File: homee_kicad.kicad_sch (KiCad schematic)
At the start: 22 parts, among them J1 Screw_Terminal_01x02, J2 476421001, J3 Screw_Terminal_01x02, K1 ORWH-SH-105D1F,000, Q1 2N7002, U1 ESP-01v090, U2 LD1117S33TR_SOT223, U4 PC817

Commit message: schema final rework
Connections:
- net 5V is gone; now on net +5V: BC1.3 (VCC_OUT), C1.2, D7.1 (K), K1.2 (COIL_1), R9.2, U2.3 (VI)
- net GND: now also Q1.2 (S); no longer Q1.3 (D)
- net at D7.2 (A), D8.1 (K), K1.4 (COIL_2): now also Q1.3 (D); no longer Q1.2 (S)
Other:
- moved on the sheet: D7, D8, J3, K1, Q1, R7, R8, R9, U4

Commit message: oupsi
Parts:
- BC1: footprint Connect:Buck Connect -> Homme:Buck Connect
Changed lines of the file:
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@@
 			)
 		)
-		(property "Footprint" "Connect:Buck Connect"
+		(property "Footprint" "Homme:Buck Connect"
 			(at 140.97 130.81 0)
 			(effects

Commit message: Change IO disposition
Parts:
- removed J1, J3: Screw_Terminal_01x02, TerminalBlock_Phoenix:TerminalBlock_Phoenix_MKDS-1,5-2-5.08_1x02_P5.08mm_Horizontal, symbol Connector:Screw_Terminal_01x02
- removed K1: ORWH-SH-105D1F,000, Homme:ORWH-1T, symbol ORWH-SH-105D1F_000:ORWH-SH-105D1F,000
- added J1: Screw_Terminal_01x04, symbol Connector:Screw_Terminal_01x04
- added K2: SANYOU_SRD_Form_C, Relay_THT:Relay_SPDT_SANYOU_SRD_Series_Form_C, symbol Relay:SANYOU_SRD_Form_C
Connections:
- net +5V: now also K2.2
- net L IN: now also J1.3 (Pin_3), K2.1
- net N IN: now also J1.1 (Pin_1)
- net at D7.2 (A), D8.1 (K), Q1.3 (D): now also K2.5
- new net NC: J1.2 (Pin_2), K2.4
- new net NO: J1.4 (Pin_4), K2.3

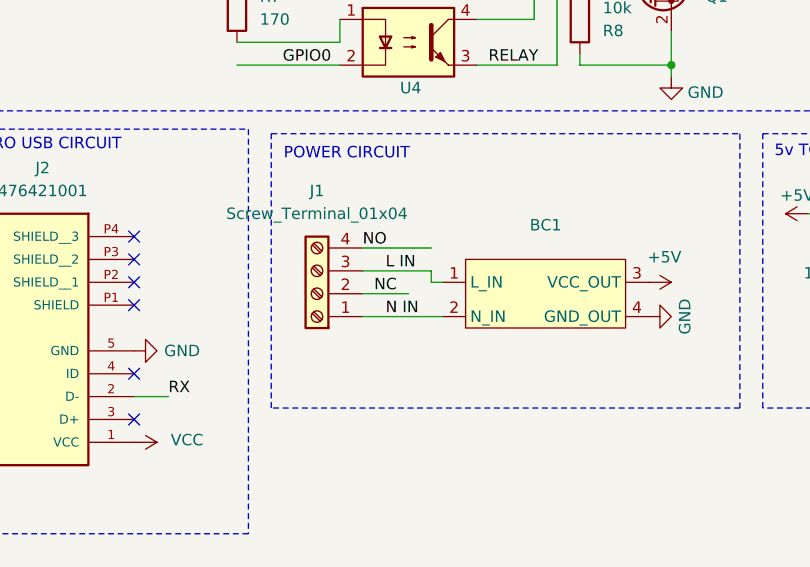
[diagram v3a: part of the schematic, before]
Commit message: UPDATED TEST W/O ROUTES
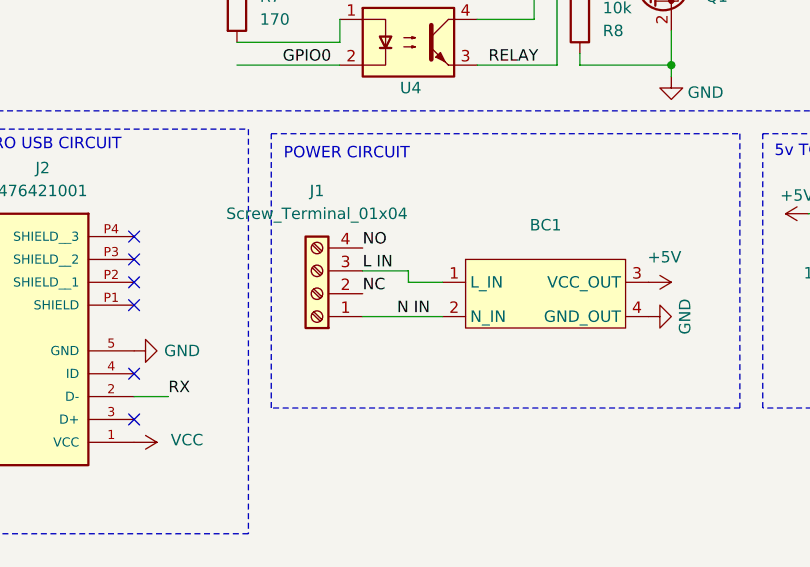
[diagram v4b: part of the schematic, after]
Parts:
- J1: footprint (none) -> TerminalBlock_Phoenix:TerminalBlock_Phoenix_PT-1,5-4-3.5-H_1x04_P3.50mm_Horizontal
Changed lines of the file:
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@@
+	(wire
+		(pts
+			(xy 124.46 139.7) (xy 133.35 139.7)
+		)
+		(stroke
+			(width 0)
+			(type default)
+		)
+	)
 	(wire
 		(pts
@@
 	(wire
 		(pts
-			(xy 132.08 132.08) (xy 124.46 132.08)
-		)
-		(stroke
-			(width 0)
-			(type default)
-		)
-	)
-	(wire
-		(pts
 			(xy 179.07 60.96) (xy 179.07 66.04)
 		)
@@
 	(wire
 		(pts
-			(xy 132.08 135.89) (xy 133.35 135.89)
-		)
-		(stroke
-			(width 0)
-			(type default)
-		)
-	)
-	(wire
-		(pts
-			(xy 132.08 134.62) (xy 132.08 135.89)
-		)
-		(stroke
-			(width 0)
-			(type default)
-		)
-	)
-	(wire
-		(pts
 			(xy 158.75 111.76) (xy 158.75 107.95)
 		)
@@
 	(wire
 		(pts
-			(xy 124.46 139.7) (xy 133.35 139.7)
-		)
-		(stroke
-			(width 0)
-			(type default)
-		)
-	)
-	(wire
-		(pts
 			(xy 148.59 102.87) (xy 151.13 102.87)
 		)
@@
 	(wire
 		(pts
+			(xy 129.54 135.89) (xy 133.35 135.89)
+		)
+		(stroke
+			(width 0)
+			(type default)
+		)
+	)
+	(wire
+		(pts
 			(xy 148.59 102.87) (xy 146.05 102.87)
 		)
@@
 	(wire
 		(pts
-			(xy 124.46 134.62) (xy 132.08 134.62)
-		)
-		(stroke
-			(width 0)
-			(type default)
-		)
-	)
-	(wire
-		(pts
 			(xy 110.49 109.22) (xy 121.92 109.22)
 		)
@@
 	(wire
 		(pts
-			(xy 129.54 137.16) (xy 124.46 137.16)
-		)
-		(stroke
-			(width 0)
-			(type default)
-		)
-	)
-	(wire
-		(pts
 			(xy 191.77 110.49) (xy 191.77 107.95)
 		)
@@
 		(pts
 			(xy 158.75 86.36) (xy 158.75 82.55)
+		)
+		(stroke
+			(width 0)
+			(type default)
+		)
+	)
+	(wire
+		(pts
+			(xy 129.54 134.62) (xy 129.54 135.89)
+		)
+		(stroke
+			(width 0)
+			(type default)
+		)
+	)
+	(wire
+		(pts
+			(xy 124.46 134.62) (xy 129.54 134.62)
 		)
 		(stroke
@@
 	)
 	(label "NC"
-		(at 125.73 137.16 0)
-		(fields_autoplaced yes)
-		(effects
-			(font
-				(size 1.27 1.27)
-			)
-			(justify left bottom)
-		)
-	)
-	(label "N IN"
-		(at 127 139.7 0)
+		(at 124.46 137.16 0)
 		(fields_autoplaced yes)
 		(effects
@@
 	)
 	(label "L IN"
-		(at 127 134.62 0)
+		(at 124.46 134.62 0)
+		(fields_autoplaced yes)
+		(effects
+			(font
+				(size 1.27 1.27)
+			)
+			(justify left bottom)
+		)
+	)
+	(label "N IN"
+		(at 128.27 139.7 0)
 		(fields_autoplaced yes)
 		(effects
@@
 			)
 		)
-		(property "Footprint" ""
+		(property "Footprint" "TerminalBlock_Phoenix:TerminalBlock_Phoenix_PT-1,5-4-3.5-H_1x04_P3.50mm_Horizontal"
 			(at 119.38 137.16 0)
 			(effects

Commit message: JOB'S FINISHED ? JOB'S NOT FINISHED
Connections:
- net L IN: now also J1.2 (Pin_2); no longer J1.3 (Pin_3)
- net N IN: now also J1.4 (Pin_4); no longer J1.1 (Pin_1)
- net NC: now also J1.3 (Pin_3); no longer J1.2 (Pin_2)
- net NO: now also J1.1 (Pin_1); no longer J1.4 (Pin_4)
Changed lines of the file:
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@@
-	(wire
-		(pts
-			(xy 124.46 139.7) (xy 133.35 139.7)
-		)
-		(stroke
-			(width 0)
-			(type default)
-		)
-	)
 	(wire
 		(pts
@@
 	(wire
 		(pts
-			(xy 129.54 135.89) (xy 133.35 135.89)
-		)
-		(stroke
-			(width 0)
-			(type default)
-		)
-	)
-	(wire
-		(pts
 			(xy 148.59 102.87) (xy 146.05 102.87)
 		)
@@
 	(wire
 		(pts
+			(xy 133.35 137.16) (xy 133.35 135.89)
+		)
+		(stroke
+			(width 0)
+			(type default)
+		)
+	)
+	(wire
+		(pts
 			(xy 179.07 55.88) (xy 184.15 55.88)
 		)
@@
 	(wire
 		(pts
+			(xy 124.46 137.16) (xy 133.35 137.16)
+		)
+		(stroke
+			(width 0)
+			(type default)
+		)
+	)
+	(wire
+		(pts
 			(xy 146.05 102.87) (xy 146.05 111.76)
 		)
@@
 	(wire
 		(pts
+			(xy 124.46 132.08) (xy 130.81 132.08)
+		)
+		(stroke
+			(width 0)
+			(type default)
+		)
+	)
+	(wire
+		(pts
 			(xy 143.51 101.6) (xy 143.51 106.68)
 		)
@@
 	(wire
 		(pts
+			(xy 130.81 139.7) (xy 133.35 139.7)
+		)
+		(stroke
+			(width 0)
+			(type default)
+		)
+	)
+	(wire
+		(pts
 			(xy 110.49 109.22) (xy 121.92 109.22)
 		)
@@
 	(wire
 		(pts
+			(xy 130.81 132.08) (xy 130.81 139.7)
+		)
+		(stroke
+			(width 0)
+			(type default)
+		)
+	)
+	(wire
+		(pts
 			(xy 176.53 128.27) (xy 176.53 133.35)
 		)
@@
 		(pts
 			(xy 158.75 86.36) (xy 158.75 82.55)
-		)
-		(stroke
-			(width 0)
-			(type default)
-		)
-	)
-	(wire
-		(pts
-			(xy 129.54 134.62) (xy 129.54 135.89)
-		)
-		(stroke
-			(width 0)
-			(type default)
-		)
-	)
-	(wire
-		(pts
-			(xy 124.46 134.62) (xy 129.54 134.62)
 		)
 		(stroke
@@
 	)
 	(label "NO"
-		(at 124.46 132.08 0)
+		(at 124.46 139.7 0)
 		(fields_autoplaced yes)
 		(effects
@@
 	)
 	(label "NC"
-		(at 124.46 137.16 0)
+		(at 124.46 134.62 0)
 		(fields_autoplaced yes)
 		(effects
@@
 	)
 	(label "L IN"
-		(at 124.46 134.62 0)
+		(at 124.46 137.16 0)
 		(fields_autoplaced yes)
 		(effects
@@
 	)
 	(label "N IN"
-		(at 128.27 139.7 0)
-		(fields_autoplaced yes)
-		(effects
+		(at 124.46 132.08 0)
+		(fields_autoplaced yes)
+		(effects

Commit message: PLZ BE THE LAST TIME :'(
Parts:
- J1: footprint TerminalBlock_Phoenix:TerminalBlock_Phoenix_PT-1,5-4-3.5-H_1x04_P3.50mm_Horizontal -> TerminalBlock:TerminalBlock_Xinya_XY308-2.54-4P_1x04_P2.54mm_Horizontal
- R1, R7: footprint Homme:ERJUP6 -> Resistor_SMD:R_0805_2012Metric_Pad1.20x1.40mm_HandSolder
- R4, R5, R6, R8, R9: footprint Homme:RESC6332X70N -> Resistor_SMD:R_0805_2012Metric_Pad1.20x1.40mm_HandSolder
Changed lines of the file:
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@@
 			)
 		)
-		(property "Footprint" "Homme:RESC6332X70N"
+		(property "Footprint" "Resistor_SMD:R_0805_2012Metric_Pad1.20x1.40mm_HandSolder"
 			(at 187.96 62.738 90)
 			(effects
@@
 			)
 		)
-		(property "Footprint" "Homme:ERJUP6"
+		(property "Footprint" "Resistor_SMD:R_0805_2012Metric_Pad1.20x1.40mm_HandSolder"
 			(at 108.712 105.41 90)
 			(effects
@@
 			)
 		)
-		(property "Footprint" "TerminalBlock_Phoenix:TerminalBlock_Phoenix_PT-1,5-4-3.5-H_1x04_P3.50mm_Horizontal"
+		(property "Footprint" "TerminalBlock:TerminalBlock_Xinya_XY308-2.54-4P_1x04_P2.54mm_Horizontal"
 			(at 119.38 137.16 0)
 			(effects
@@
 			)
 		)
-		(property "Footprint" "Homme:RESC6332X70N"
+		(property "Footprint" "Resistor_SMD:R_0805_2012Metric_Pad1.20x1.40mm_HandSolder"
 			(at 187.96 67.818 90)
 			(effects
@@
 			)
 		)
-		(property "Footprint" "Homme:ERJUP6"
+		(property "Footprint" "Resistor_SMD:R_0805_2012Metric_Pad1.20x1.40mm_HandSolder"
 			(at 189.992 93.98 90)
 			(effects
@@
 			)
 		)
-		(property "Footprint" "Homme:RESC6332X70N"
+		(property "Footprint" "Resistor_SMD:R_0805_2012Metric_Pad1.20x1.40mm_HandSolder"
 			(at 187.96 57.658 90)
 			(effects
@@
 			)
 		)
-		(property "Footprint" "Homme:RESC6332X70N"
+		(property "Footprint" "Resistor_SMD:R_0805_2012Metric_Pad1.20x1.40mm_HandSolder"
 			(at 146.812 106.68 90)
 			(effects
@@
 			)
 		)
-		(property "Footprint" "Homme:RESC6332X70N"
+		(property "Footprint" "Resistor_SMD:R_0805_2012Metric_Pad1.20x1.40mm_HandSolder"
 			(at 168.402 86.36 90)
 			(effects
